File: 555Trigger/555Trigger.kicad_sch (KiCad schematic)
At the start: 11 parts, among them J1 Conn_01x03_Socket, J2 Timing Signal Out, J3 Timing Signal In, U1 L272, U2 TLC555xP

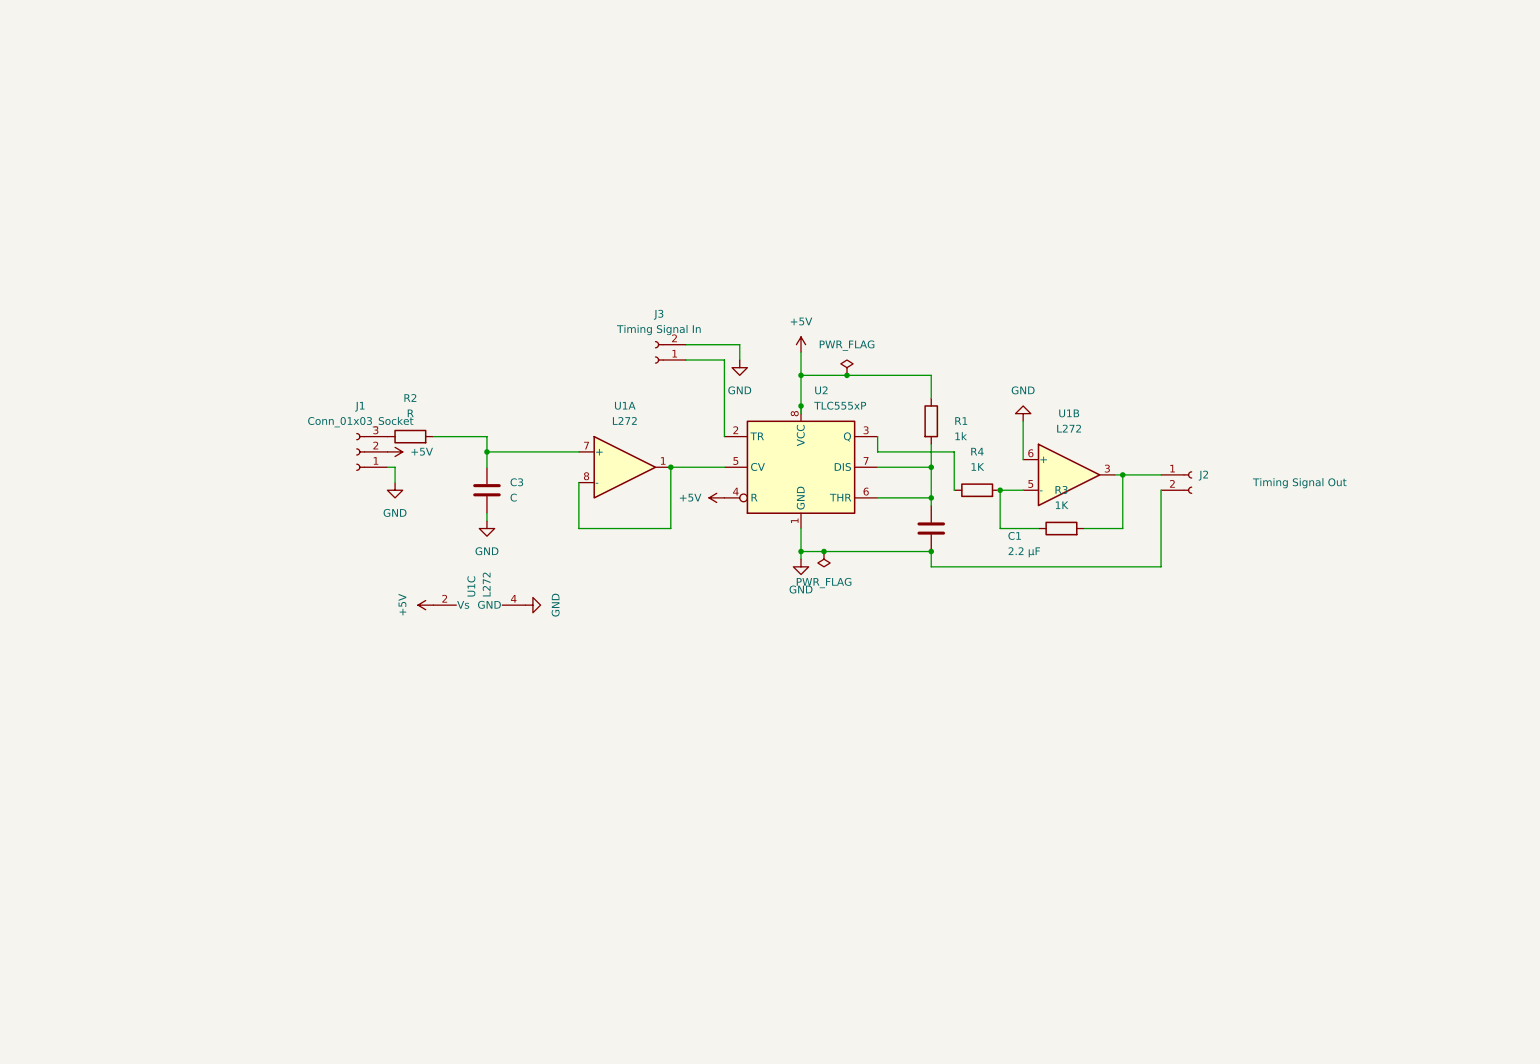
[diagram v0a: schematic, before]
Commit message: Added subsystems for master board
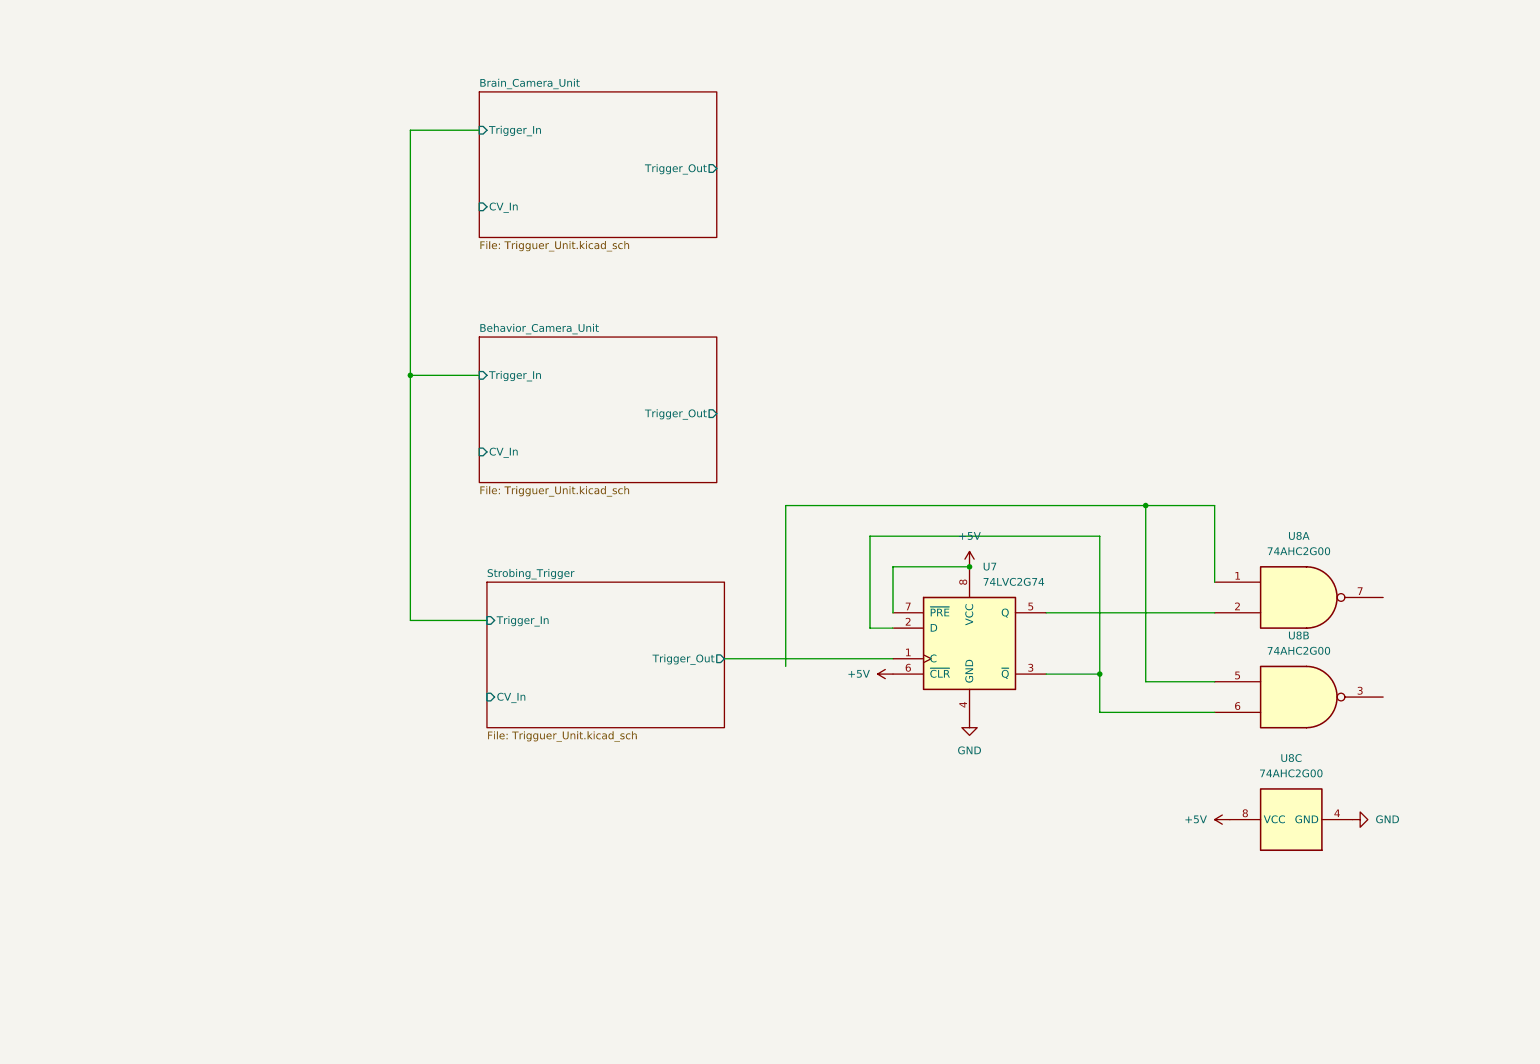
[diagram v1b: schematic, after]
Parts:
- removed C1: 2.2 μF, Capacitor_THT:CP_Axial_L10.0mm_D4.5mm_P15.00mm_Horizontal, symbol Device:C
- removed C3: C, Capacitor_THT:CP_Axial_L10.0mm_D4.5mm_P15.00mm_Horizontal, symbol Device:C
- removed J1: Conn_01x03_Socket, Connector_JST:JST_EH_B3B-EH-A_1x03_P2.50mm_Vertical, symbol Connector:Conn_01x03_Socket
- removed J2: Timing Signal Out, Connector_JST:JST_EH_B2B-EH-A_1x02_P2.50mm_Vertical, symbol Connector:Conn_01x02_Socket
- removed J3: Timing Signal In, Connector_JST:JST_EH_B2B-EH-A_1x02_P2.50mm_Vertical, symbol Connector:Conn_01x02_Socket
- removed R1: 1k, Resistor_THT:R_Axial_DIN0204_L3.6mm_D1.6mm_P5.08mm_Horizontal, symbol Device:R
- removed R2: R, Resistor_THT:R_Axial_DIN0204_L3.6mm_D1.6mm_P5.08mm_Horizontal, symbol Device:R
- removed R3, R4: 1K, Resistor_THT:R_Axial_DIN0204_L3.6mm_D1.6mm_P5.08mm_Horizontal, symbol Device:R
- removed U1: L272, Package_DIP:DIP-16_W7.62mm, symbol Amplifier_Operational:L272
- removed U2: TLC555xP, Package_DIP:DIP-8_W7.62mm, symbol Timer:TLC555xP
- added U7: 74LVC2G74, Package_TO_SOT_SMD:SOT-223-6_TabPin3, symbol 74xGxx:74LVC2G74
- added U8: 74AHC2G00, symbol 74xGxx:74AHC2G00
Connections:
- net +5V: now also U7.6 (~{CLR}), U7.7 (~{PRE}), U7.8 (VCC), U8.8 (VCC)
- net GND: now also U7.4 (GND), U8.4 (GND)
- new net: U8.1, U8.5
- new net: U7.2 (D), U7.3 (~{Q}), U8.6
- new net: U7.5 (Q), U8.2
- new net Strobing_Trigger/Trigger_Out: U7.1 (C)
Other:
- added sheet Behavior_Camera_Unit (Trigguer_Unit.kicad_sch)
- added sheet Brain_Camera_Unit (Trigguer_Unit.kicad_sch)
- added sheet Strobing_Trigger (Trigguer_Unit.kicad_sch)

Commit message: changed to SMD
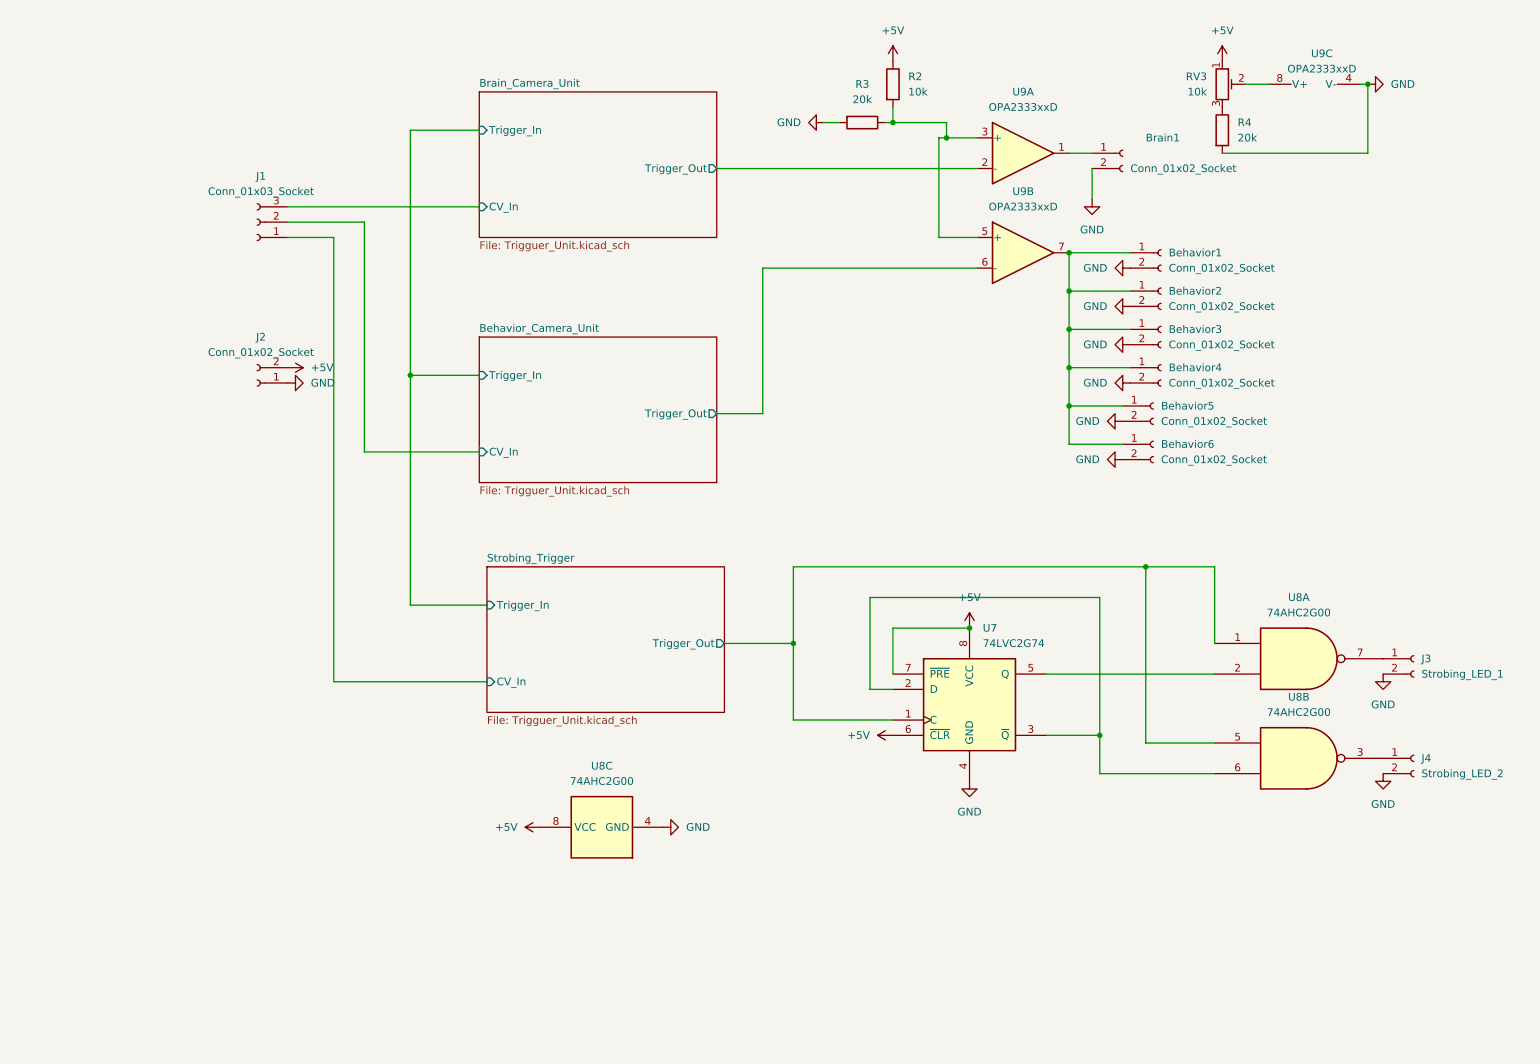
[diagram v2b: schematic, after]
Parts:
- added Behavior1, Behavior2, Behavior3, Behavior4, Behavior5, Behavior6, Brain1, J2: Conn_01x02_Socket, Connector_JST:JST_EH_B2B-EH-A_1x02_P2.50mm_Vertical, symbol Connector:Conn_01x02_Socket
- added J1: Conn_01x03_Socket, Connector_JST:JST_EH_B3B-EH-A_1x03_P2.50mm_Vertical, symbol Connector:Conn_01x03_Socket
- added J3: Strobing_LED_1, Connector_JST:JST_EH_B2B-EH-A_1x02_P2.50mm_Vertical, symbol Connector:Conn_01x02_Socket
- added J4: Strobing_LED_2, Connector_JST:JST_EH_B2B-EH-A_1x02_P2.50mm_Vertical, symbol Connector:Conn_01x02_Socket
- added R2: 10k, Resistor_SMD:R_0805_2012Metric_Pad1.20x1.40mm_HandSolder, symbol Device:R
- added R3, R4: 20k, Resistor_SMD:R_0805_2012Metric_Pad1.20x1.40mm_HandSolder, symbol Device:R
- added RV3: 10k, Potentiometer_SMD:Potentiometer_ACP_CA14-VSMD_Vertical_Hole, symbol Device:R_Potentiometer_Trim
- added U9: OPA2333xxD, Package_SO:OnSemi_Micro8, symbol Amplifier_Operational:OPA2333xxD
- U8: footprint (none) -> Package_SO:VSSOP-8_2.3x2mm_P0.5mm
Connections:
- net +5V: now also J2.2 (Pin_2), R2.1, RV3.1
- net Behavior_Camera_Unit/CV_In: now also J1.2 (Pin_2)
- net Behavior_Camera_Unit/Trigger_Out: now also U9.6 (-)
- net Brain_Camera_Unit/CV_In: now also J1.3 (Pin_3)
- net Brain_Camera_Unit/Trigger_Out: now also U9.2 (-)
- net GND: now also Behavior1.2 (Pin_2), Behavior2.2 (Pin_2), Behavior3.2 (Pin_2), Behavior4.2 (Pin_2), Behavior5.2 (Pin_2), Behavior6.2 (Pin_2), Brain1.2 (Pin_2), J2.1 (Pin_1), J3.2 (Pin_2), J4.2 (Pin_2), R3.2, R4.2, U9.4 (V-)
- net Strobing_Trigger/CV_In: now also J1.1 (Pin_1)
- net Strobing_Trigger/Trigger_Out: now also U8.1, U8.5
- net at U8.3: now also J4.1 (Pin_1)
- net at U8.7: now also J3.1 (Pin_1)
- new net: Behavior1.1 (Pin_1), Behavior2.1 (Pin_1), Behavior3.1 (Pin_1), Behavior4.1 (Pin_1), Behavior5.1 (Pin_1), Behavior6.1 (Pin_1), U9.7
- new net: R4.1, RV3.3
- new net: Brain1.1 (Pin_1), U9.1
- new net: R2.2, R3.1, U9.3 (+), U9.5 (+)
- new net: RV3.2, U9.8 (V+)
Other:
- moved on the sheet: U7, U8A, U8B, U8C

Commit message: updated timer design
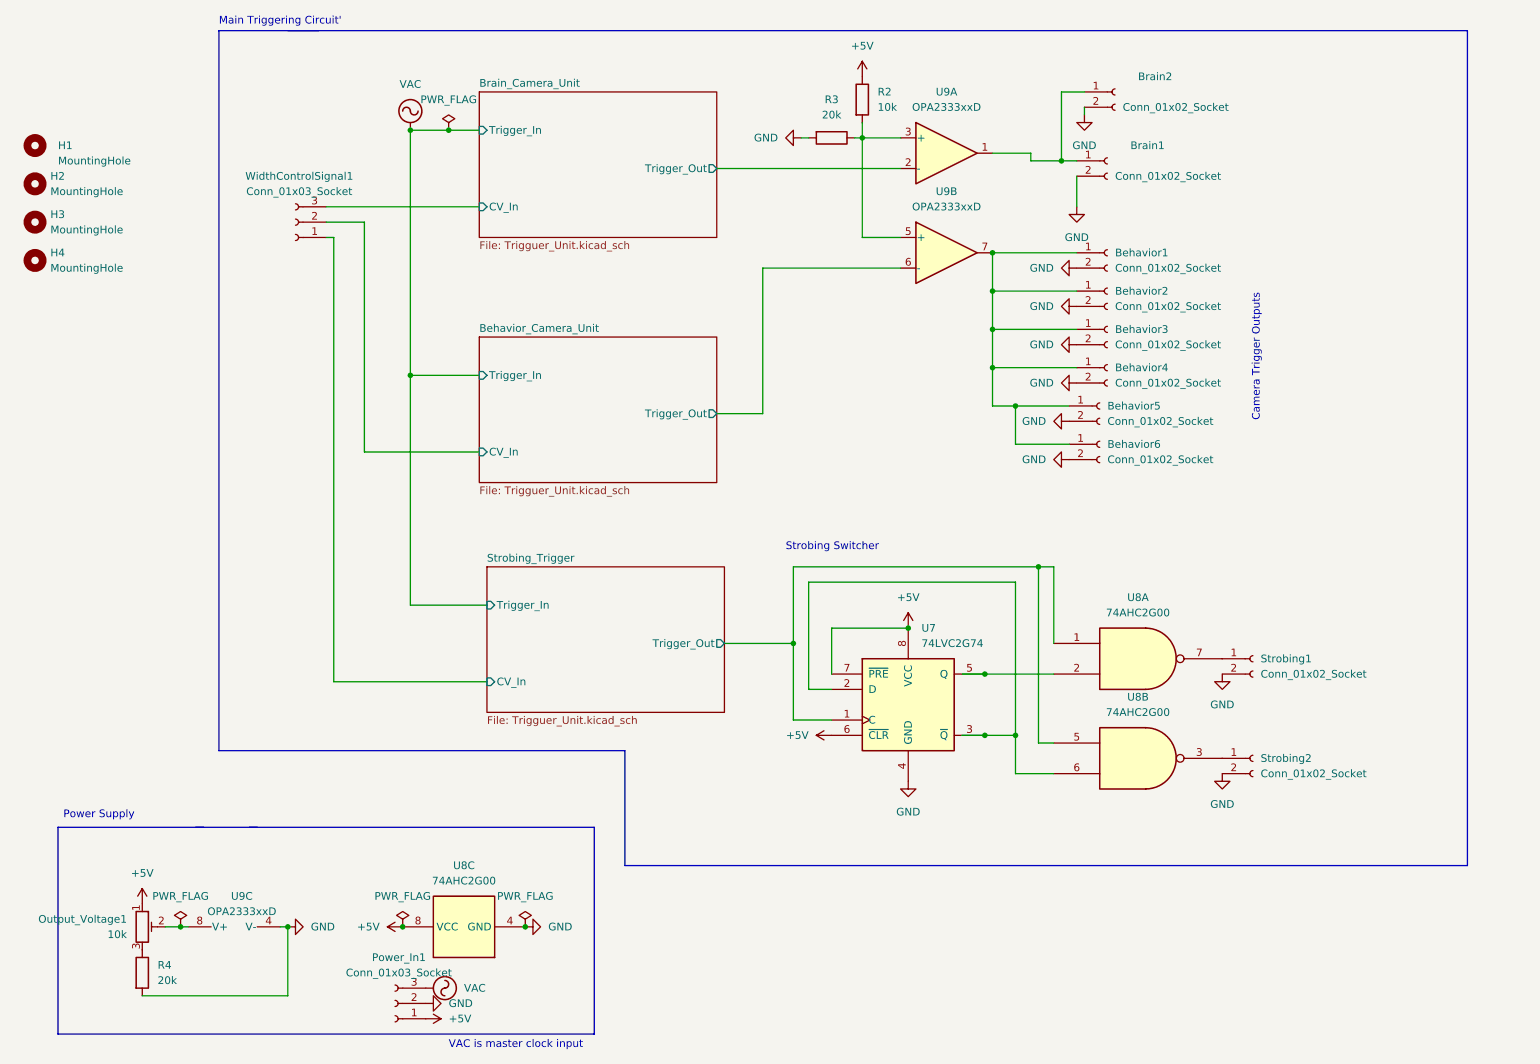
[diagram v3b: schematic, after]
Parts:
- removed J2: Conn_01x02_Socket, Connector_JST:JST_EH_B2B-EH-A_1x02_P2.50mm_Vertical, symbol Connector:Conn_01x02_Socket
- added Brain2: Conn_01x02_Socket, Connector_JST:JST_EH_S2B-EH_1x02_P2.50mm_Horizontal, symbol Connector:Conn_01x02_Socket
- added H1, H2, H3, H4: MountingHole, MountingHole:MountingHole_2.2mm_M2, symbol Mechanical:MountingHole
- added Power_In1: Conn_01x03_Socket, Connector_JST:JST_XA_B03B-XASK-1-A_1x03_P2.50mm_Vertical, symbol Connector:Conn_01x03_Socket
- Behavior1, Behavior2, Behavior3, Behavior4, Behavior5, Behavior6, Brain1: footprint Connector_JST:JST_EH_B2B-EH-A_1x02_P2.50mm_Vertical -> Connector_JST:JST_EH_S2B-EH_1x02_P2.50mm_Horizontal
- Output_Voltage1: renamed from RV3; footprint Potentiometer_SMD:Potentiometer_ACP_CA14-VSMD_Vertical_Hole -> Potentiometer_SMD:Potentiometer_ACP_CA9-VSMD_Vertical
- Strobing1: renamed from J3; value Strobing_LED_1 -> Conn_01x02_Socket; footprint Connector_JST:JST_EH_B2B-EH-A_1x02_P2.50mm_Vertical -> Connector_JST:JST_EH_S2B-EH_1x02_P2.50mm_Horizontal
- Strobing2: renamed from J4; value Strobing_LED_2 -> Conn_01x02_Socket; footprint Connector_JST:JST_EH_B2B-EH-A_1x02_P2.50mm_Vertical -> Connector_JST:JST_EH_S2B-EH_1x02_P2.50mm_Horizontal
- U7: footprint Package_TO_SOT_SMD:SOT-223-6_TabPin3 -> Package_SO:SSOP-8_2.95x2.8mm_P0.65mm
- U9: footprint Package_SO:OnSemi_Micro8 -> Package_DIP:DIP-8_W7.62mm_SMDSocket_SmallPads
- WidthControlSignal1: renamed from J1; footprint Connector_JST:JST_EH_B3B-EH-A_1x03_P2.50mm_Vertical -> Connector_JST:JST_XA_B03B-XASK-1-A_1x03_P2.50mm_Vertical
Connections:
- net +5V: now also Power_In1.1 (Pin_1)
- net GND: now also Brain2.2 (Pin_2), Power_In1.2 (Pin_2)
- net at Brain1.1 (Pin_1), U9.1: now also Brain2.1 (Pin_1)
- new net VAC: Power_In1.3 (Pin_3)
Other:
- note added: "Camera Trigger Outputs"
- note added: "Main Triggering Circuit'"
- note added: "Power Supply"
- note added: "Strobing Switcher"
- note added: "VAC is master clock input"
- moved on the sheet: Behavior1, Behavior2, Behavior3, Behavior4, Behavior5, Behavior6, Brain1, Output_Voltage1, R2, R3, R4, Strobing1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
